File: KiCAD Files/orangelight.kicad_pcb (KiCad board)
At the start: 2 copper layers, 17.5 x 26 mm, 6 parts, among them J1 REV_JST_SMD, J2 REV_JST_SMD, U1 K230_Rewired, U2 ZDSD04GLGEAG, U3 HC-FPC-0_5-22P-CXH20, U4 K4E8E324ED-EGCG

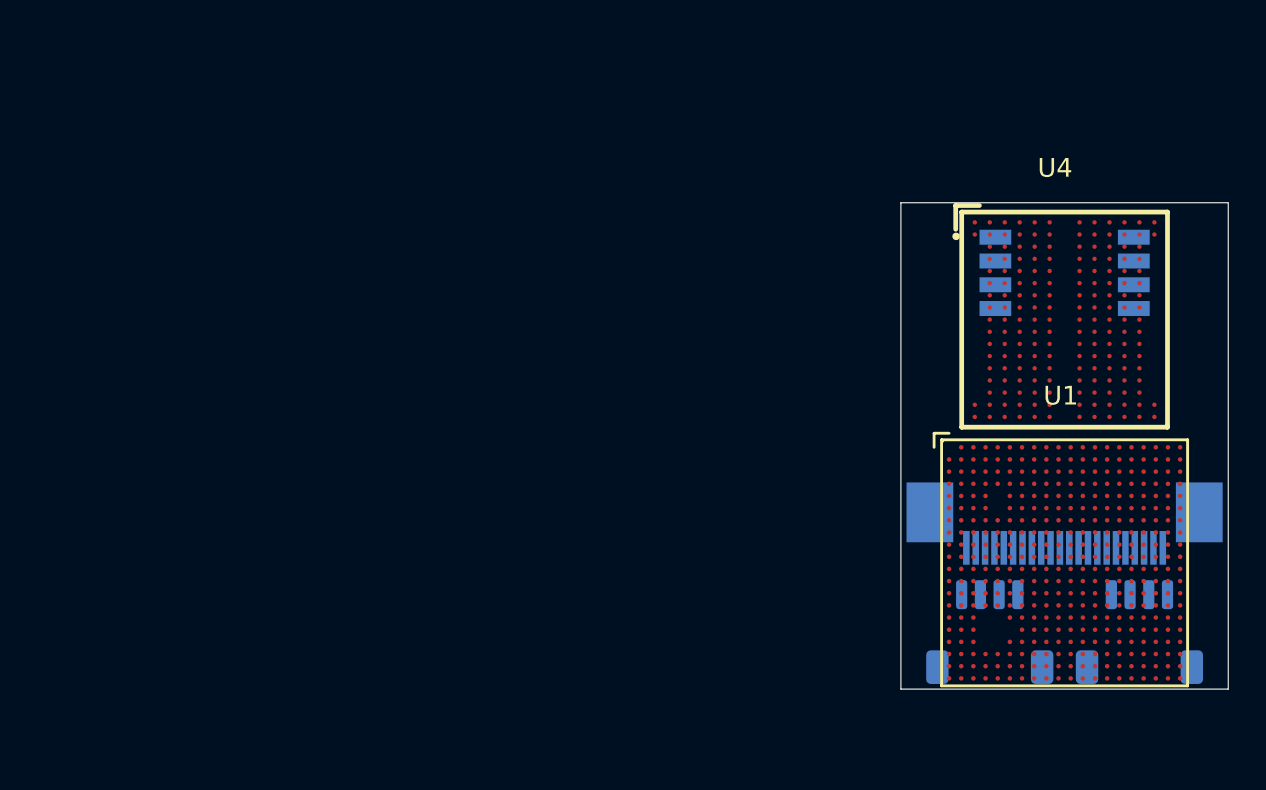
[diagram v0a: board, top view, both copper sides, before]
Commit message: more peripherals
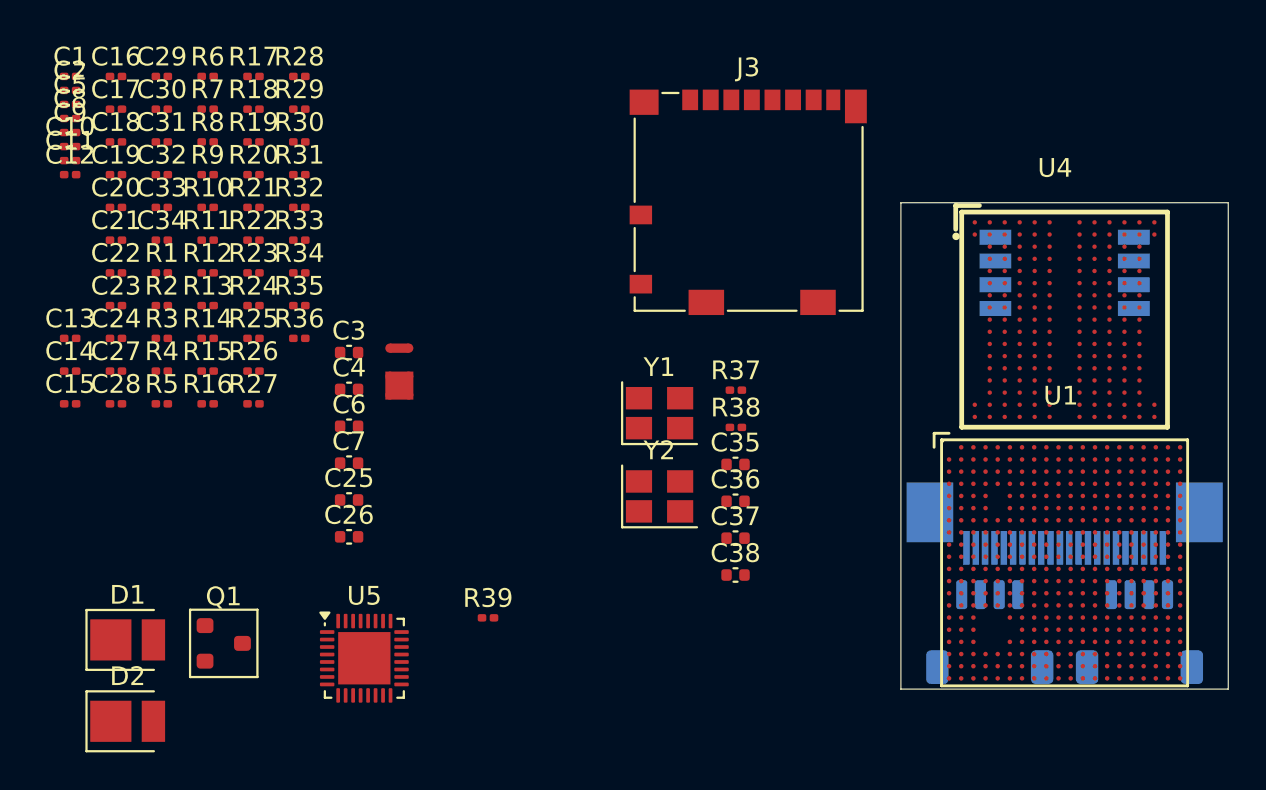
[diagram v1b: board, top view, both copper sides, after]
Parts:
- added C1: 100nF, Capacitor_SMD:C_0201_0603Metric, F.Cu at (-53.2, -26.0)
- added C10: 100nF, Capacitor_SMD:C_0201_0603Metric, F.Cu at (-53.2, -22.2)
- added C11: 100nF, Capacitor_SMD:C_0201_0603Metric, F.Cu at (-53.2, -21.5)
- added C12: 100nF, Capacitor_SMD:C_0201_0603Metric, F.Cu at (-53.2, -20.8)
- added C13: 100nF, Capacitor_SMD:C_0201_0603Metric, F.Cu at (-53.2, -12.0)
- added C14: 100nF, Capacitor_SMD:C_0201_0603Metric, F.Cu at (-53.2, -10.2)
- added C15: 100nF, Capacitor_SMD:C_0201_0603Metric, F.Cu at (-53.2, -8.50)
- added C16: 100nF, Capacitor_SMD:C_0201_0603Metric, F.Cu at (-50.7, -26.0)
- added C17: 100nF, Capacitor_SMD:C_0201_0603Metric, F.Cu at (-50.7, -24.2)
- added C18: 100nF, Capacitor_SMD:C_0201_0603Metric, F.Cu at (-50.7, -22.5)
- added C19: 100nF, Capacitor_SMD:C_0201_0603Metric, F.Cu at (-50.7, -20.8)
- added C2: 100nF, Capacitor_SMD:C_0201_0603Metric, F.Cu at (-53.2, -25.2)
- added C20: 100nF, Capacitor_SMD:C_0201_0603Metric, F.Cu at (-50.7, -19.0)
- added C21: 100nF, Capacitor_SMD:C_0201_0603Metric, F.Cu at (-50.7, -17.2)
- added C22: 100nF, Capacitor_SMD:C_0201_0603Metric, F.Cu at (-50.7, -15.5)
- added C23: 100nF, Capacitor_SMD:C_0201_0603Metric, F.Cu at (-50.7, -13.8)
- added C24: 100nF, Capacitor_SMD:C_0201_0603Metric, F.Cu at (-50.7, -12.0)
- added C25: 22uF, Capacitor_SMD:C_0402_1005Metric, F.Cu at (-38.2, -3.36)
- added C26: 4.7uF, Capacitor_SMD:C_0402_1005Metric, F.Cu at (-38.2, -1.39)
- added C27: 100nF, Capacitor_SMD:C_0201_0603Metric, F.Cu at (-50.7, -10.2)
- added C28: 100nF, Capacitor_SMD:C_0201_0603Metric, F.Cu at (-50.7, -8.50)
- added C29: 100nF, Capacitor_SMD:C_0201_0603Metric, F.Cu at (-48.3, -26.0)
- added C3: 22uF, Capacitor_SMD:C_0402_1005Metric, F.Cu at (-38.2, -11.2)
- added C30: 100nF, Capacitor_SMD:C_0201_0603Metric, F.Cu at (-48.3, -24.2)
- added C31: 100nF, Capacitor_SMD:C_0201_0603Metric, F.Cu at (-48.3, -22.5)
- added C32: 100nF, Capacitor_SMD:C_0201_0603Metric, F.Cu at (-48.3, -20.8)
- added C33: 100nF, Capacitor_SMD:C_0201_0603Metric, F.Cu at (-48.3, -19.0)
- added C34: 100nF, Capacitor_SMD:C_0201_0603Metric, F.Cu at (-48.3, -17.2)
- added C35: 15pF, Capacitor_SMD:C_0402_1005Metric, F.Cu at (-17.6, -5.26)
- added C36: 15pF, Capacitor_SMD:C_0402_1005Metric, F.Cu at (-17.6, -3.29)
- added C37: 15pF, Capacitor_SMD:C_0402_1005Metric, F.Cu at (-17.6, -1.32)
- added C38: 15pF, Capacitor_SMD:C_0402_1005Metric, F.Cu at (-17.6, 0.65)
- added C4: 4.7uF, Capacitor_SMD:C_0402_1005Metric, F.Cu at (-38.2, -9.27)
- added C5: 100nF, Capacitor_SMD:C_0201_0603Metric, F.Cu at (-53.2, -24.5)
- added C6: 22uF, Capacitor_SMD:C_0402_1005Metric, F.Cu at (-38.2, -7.30)
- added C7: 4.7uF, Capacitor_SMD:C_0402_1005Metric, F.Cu at (-38.2, -5.33)
- added C8: 100nF, Capacitor_SMD:C_0201_0603Metric, F.Cu at (-53.2, -23.8)
- added C9: 100nF, Capacitor_SMD:C_0201_0603Metric, F.Cu at (-53.2, -23.0)
- added D1: LED, LED_SMD:LED_PLCC_2835, F.Cu at (-50.1, 4.12)
- added D2: LED, LED_SMD:LED_PLCC_2835, F.Cu at (-50.1, 8.47)
- added J3: Micro_SD_Card_Det2, Connector_Card:microSD_HC_Molex_104031-0811, F.Cu at (-16.9, -19.3)
- added NT1: NetTie_2, NetTie:NetTie-2_SMD_Pad0.5mm, F.Cu at (-35.6, -11.5)
- added NT2: NetTie_4, NetTie:NetTie-4_SMD_Pad0.5mm, F.Cu at (-35.6, -9.47)
- added Q1: 2N7002, PCM_Package_TO_SOT_SMD_AKL:SOT-23, F.Cu at (-44.9, 4.30)
- added R1: 240R, Resistor_SMD:R_0201_0603Metric, F.Cu at (-48.3, -15.5)
- added R10: 120R, Resistor_SMD:R_0201_0603Metric, F.Cu at (-45.8, -19.0)
- added R11: 120R, Resistor_SMD:R_0201_0603Metric, F.Cu at (-45.8, -17.2)
- added R12: 120R, Resistor_SMD:R_0201_0603Metric, F.Cu at (-45.8, -15.5)
- added R13: 120R, Resistor_SMD:R_0201_0603Metric, F.Cu at (-45.8, -13.8)
- added R14: 120R, Resistor_SMD:R_0201_0603Metric, F.Cu at (-45.8, -12.0)
- added R15: 120R, Resistor_SMD:R_0201_0603Metric, F.Cu at (-45.8, -10.2)
- added R16: 120R, Resistor_SMD:R_0201_0603Metric, F.Cu at (-45.8, -8.50)
- added R17: 120R, Resistor_SMD:R_0201_0603Metric, F.Cu at (-43.4, -26.0)
- added R18: 120R, Resistor_SMD:R_0201_0603Metric, F.Cu at (-43.4, -24.2)
- added R19: 120R, Resistor_SMD:R_0201_0603Metric, F.Cu at (-43.4, -22.5)
- added R2: 240R, Resistor_SMD:R_0201_0603Metric, F.Cu at (-48.3, -13.8)
- added R20: 120R, Resistor_SMD:R_0201_0603Metric, F.Cu at (-43.4, -20.8)
- added R21: 120R, Resistor_SMD:R_0201_0603Metric, F.Cu at (-43.4, -19.0)
- added R22: 120R, Resistor_SMD:R_0201_0603Metric, F.Cu at (-43.4, -17.2)
- added R23: 120R, Resistor_SMD:R_0201_0603Metric, F.Cu at (-43.4, -15.5)
- added R24: 120R, Resistor_SMD:R_0201_0603Metric, F.Cu at (-43.4, -13.8)
- added R25: 120R, Resistor_SMD:R_0201_0603Metric, F.Cu at (-43.4, -12.0)
- added R26: 120R, Resistor_SMD:R_0201_0603Metric, F.Cu at (-43.4, -10.2)
- added R27: 120R, Resistor_SMD:R_0201_0603Metric, F.Cu at (-43.4, -8.50)
- added R28: 120R, Resistor_SMD:R_0201_0603Metric, F.Cu at (-40.9, -26.0)
- added R29: 120R, Resistor_SMD:R_0201_0603Metric, F.Cu at (-40.9, -24.2)
- added R3: 120R, Resistor_SMD:R_0201_0603Metric, F.Cu at (-48.3, -12.0)
- added R30: 120R, Resistor_SMD:R_0201_0603Metric, F.Cu at (-40.9, -22.5)
- added R31: 120R, Resistor_SMD:R_0201_0603Metric, F.Cu at (-40.9, -20.8)
- added R32: 120R, Resistor_SMD:R_0201_0603Metric, F.Cu at (-40.9, -19.0)
- added R33: 120R, Resistor_SMD:R_0201_0603Metric, F.Cu at (-40.9, -17.2)
- added R34: 120R, Resistor_SMD:R_0201_0603Metric, F.Cu at (-40.9, -15.5)
- added R35: 120R, Resistor_SMD:R_0201_0603Metric, F.Cu at (-40.9, -13.8)
- added R36: 240R, Resistor_SMD:R_0201_0603Metric, F.Cu at (-40.9, -12.0)
- added R37: 1M, Resistor_SMD:R_0201_0603Metric, F.Cu at (-17.6, -9.23)
- added R38: 1M, Resistor_SMD:R_0201_0603Metric, F.Cu at (-17.6, -7.24)
- added R39: 200R, Resistor_SMD:R_0201_0603Metric, F.Cu at (-30.8, 2.94)
- added R4: 120R, Resistor_SMD:R_0201_0603Metric, F.Cu at (-48.3, -10.2)
- added R5: 120R, Resistor_SMD:R_0201_0603Metric, F.Cu at (-48.3, -8.50)
- added R6: 120R, Resistor_SMD:R_0201_0603Metric, F.Cu at (-45.8, -26.0)
- added R7: 120R, Resistor_SMD:R_0201_0603Metric, F.Cu at (-45.8, -24.2)
- added R8: 120R, Resistor_SMD:R_0201_0603Metric, F.Cu at (-45.8, -22.5)
- added R9: 120R, Resistor_SMD:R_0201_0603Metric, F.Cu at (-45.8, -20.8)
- added U5: RT9992ZQW, Package_DFN_QFN:Texas_RSN_WQFN-32-1EP_4x4mm_P0.4mm_EP2.8x2.8mm, F.Cu at (-37.4, 5.10)
- added Y1: 32.768KHz, Crystal:Crystal_SMD_Abracon_ABM8AIG-4Pin_3.2x2.5mm, F.Cu at (-21.6, -8.00)
- added Y2: 32.768KHz, Crystal:Crystal_SMD_Abracon_ABM8AIG-4Pin_3.2x2.5mm, F.Cu at (-21.6, -3.55)
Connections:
- J1 pad 3: unconnected-(J1-3.3V-Pad3) -> +3V3
- J1 pad 4: unconnected-(J1-GND-Pad4) -> GND
- J2 pad 3: unconnected-(J2-3.3V-Pad3) -> +3V3
- J2 pad 4: unconnected-(J2-GND-Pad4) -> GND
- U2 pad 1: Net-(U1C-QSPI_D2) -> Net-(U1C-MMC0_D2)
- U2 pad 2: Net-(U1C-QSPI_D3) -> Net-(U1C-MMC0_D3)
- U2 pad 3: Net-(U1C-QSPI_CLK) -> Net-(U1C-MMC0_CLK)
- U2 pad 4: unconnected-(U2-GND-Pad4) -> GND
- U2 pad 5: Net-(U1C-QSPI_CS) -> Net-(U1C-MMC0_CMD)
- U2 pad 6: Net-(U1C-QSPI_D0) -> Net-(U1C-MMC0_D0)
- U2 pad 7: Net-(U1C-QSPI_D1) -> Net-(U1C-MMC0_D1)
- U2 pad 8: unconnected-(U2-VDD-Pad8) -> +3V3
- U4 pad A10: unconnected-(U4-VDD1-PadA10) -> DDR_VDD1
- U4 pad A11: unconnected-(U4-VDDQ-PadA11) -> DDR_VDDQ
- U4 pad A3: unconnected-(U4-VDD1-PadA3) -> DDR_VDD1
- U4 pad A4: unconnected-(U4-VDD1-PadA4) -> DDR_VDD1
- U4 pad A5: unconnected-(U4-VDD1-PadA5) -> DDR_VDD1
- U4 pad A6: unconnected-(U4-VDD1-PadA6) -> DDR_VDD1
- U4 pad A8: unconnected-(U4-VDD2-PadA8) -> DDR_VDD2
- U4 pad A9: unconnected-(U4-VDD2-PadA9) -> DDR_VDD2
- U4 pad B12: unconnected-(U4-VSSQ-PadB12) -> GND
- U4 pad B2: unconnected-(U4-VSS-PadB2) -> GND
- U4 pad B3: unconnected-(U4-ZQ-PadB3) -> Net-(U4-ZQ)
- U4 pad B5: unconnected-(U4-VSS-PadB5) -> GND
- U4 pad B6: unconnected-(U4-VSSQ-PadB6) -> GND
- U4 pad C12: unconnected-(U4-VDDQ-PadC12) -> DDR_VDDQ
- U4 pad C3: unconnected-(U4-VSSCA-PadC3) -> GND
- U4 pad C5: unconnected-(U4-VSS-PadC5) -> GND
- U4 pad C6: unconnected-(U4-VSSQ-PadC6) -> GND
- U4 pad D12: unconnected-(U4-VSSQ-PadD12) -> GND
- U4 pad D3: unconnected-(U4-VSSCA-PadD3) -> GND
- U4 pad D4: unconnected-(U4-VDD2-PadD4) -> DDR_VDD2
- U4 pad D5: unconnected-(U4-VDD2-PadD5) -> DDR_VDD2
- U4 pad D6: unconnected-(U4-VDD2-PadD6) -> DDR_VDD2
- U4 pad E12: unconnected-(U4-VDDQ-PadE12) -> DDR_VDDQ
- U4 pad E4: unconnected-(U4-VSS-PadE4) -> GND
- U4 pad E5: unconnected-(U4-VSS-PadE5) -> GND
- U4 pad E6: unconnected-(U4-VSSQ-PadE6) -> GND
- U4 pad E8: unconnected-(U4-VDDQ-PadE8) -> DDR_VDDQ
- U4 pad F12: unconnected-(U4-VSSQ-PadF12) -> GND
- U4 pad F2: unconnected-(U4-VDDCA-PadF2) -> DDR_VDDCA
- U4 pad F4: unconnected-(U4-VSSCA-PadF4) -> GND
- U4 pad F5: unconnected-(U4-VSS-PadF5) -> GND
- U4 pad F6: unconnected-(U4-VSSQ-PadF6) -> GND
- U4 pad G12: unconnected-(U4-VDDQ-PadG12) -> DDR_VDDQ
- U4 pad G2: unconnected-(U4-VDDCA-PadG2) -> DDR_VDDCA
- U4 pad G3: unconnected-(U4-VSSCA-PadG3) -> GND
- U4 pad G4: unconnected-(U4-VSSCA-PadG4) -> GND
- U4 pad G5: unconnected-(U4-VDD2-PadG5) -> DDR_VDD2
- U4 pad G6: unconnected-(U4-VSSQ-PadG6) -> GND
- U4 pad G9: unconnected-(U4-VSSQ-PadG9) -> GND
- U4 pad H10: unconnected-(U4-VSSQ-PadH10) -> GND
- U4 pad H11: unconnected-(U4-VDDQ-PadH11) -> DDR_VDDQ
- U4 pad H12: unconnected-(U4-VDD2-PadH12) -> DDR_VDD2
- U4 pad H2: unconnected-(U4-VSS-PadH2) -> GND
- U4 pad H3: unconnected-(U4-VDDCA-PadH3) -> DDR_VDDCA
- U4 pad H4: unconnected-(U4-VRef(CA)-PadH4) -> /RAM/DDR.VREF_CA
- U4 pad H5: unconnected-(U4-VDD2-PadH5) -> DDR_VDD2
- U4 pad H6: unconnected-(U4-VDD2-PadH6) -> DDR_VDD2
- U4 pad H8: unconnected-(U4-VDDQ-PadH8) -> DDR_VDDQ
- U4 pad H9: unconnected-(U4-VDDQ-PadH9) -> DDR_VDDQ
- U4 pad J10: unconnected-(U4-VDDQ-PadJ10) -> DDR_VDDQ
- U4 pad J11: unconnected-(U4-VRef(DQ)-PadJ11) -> /RAM/DDR.VREF_DQ
- U4 pad J12: unconnected-(U4-VSS-PadJ12) -> GND
- U4 pad J2: unconnected-(U4-CK_N-PadJ2) -> /RAM/DDR_CK-
- U4 pad J3: unconnected-(U4-CK_P-PadJ3) -> /RAM/DDR_CK+
- U4 pad J4: unconnected-(U4-VSSCA-PadJ4) -> GND
- U4 pad J5: unconnected-(U4-VDD2-PadJ5) -> DDR_VDD2
- U4 pad J6: unconnected-(U4-VDD2-PadJ6) -> DDR_VDD2
- U4 pad J8: unconnected-(U4-ODT(1)-PadJ8) -> /RAM/DDR.ODT
- U4 pad J9: unconnected-(U4-VDDQ-PadJ9) -> DDR_VDDQ
- U4 pad K10: unconnected-(U4-VSSQ-PadK10) -> GND
- U4 pad K11: unconnected-(U4-VDDQ-PadK11) -> DDR_VDDQ
- U4 pad K12: unconnected-(U4-VDD2-PadK12) -> DDR_VDD2
- U4 pad K2: unconnected-(U4-VSS-PadK2) -> GND
- U4 pad K3: unconnected-(U4-CKE-PadK3) -> /RAM/DDR_CKE
- U4 pad K5: unconnected-(U4-VDD2-PadK5) -> DDR_VDD2
- U4 pad K6: unconnected-(U4-VDD2-PadK6) -> DDR_VDD2
- U4 pad K8: unconnected-(U4-VDDQ-PadK8) -> DDR_VDDQ
- U4 pad L12: unconnected-(U4-VDDQ-PadL12) -> DDR_VDDQ
- U4 pad L2: unconnected-(U4-VDDCA-PadL2) -> DDR_VDDCA
- U4 pad L3: unconnected-(U4-CS_N-PadL3) -> /RAM/DDR.CS
- U4 pad L5: unconnected-(U4-VDD2-PadL5) -> DDR_VDD2
- U4 pad L6: unconnected-(U4-VSS-PadL6) -> GND
- U4 pad L9: unconnected-(U4-VSSQ-PadL9) -> GND
- U4 pad M12: unconnected-(U4-VSSQ-PadM12) -> GND
- U4 pad M2: unconnected-(U4-VDDCA-PadM2) -> DDR_VDDCA
- U4 pad M4: unconnected-(U4-VSSCA-PadM4) -> GND
- U4 pad M5: unconnected-(U4-VSSCA-PadM5) -> GND
- U4 pad M6: unconnected-(U4-VSSQ-PadM6) -> GND
- U4 pad N12: unconnected-(U4-VDDQ-PadN12) -> DDR_VDDQ
- U4 pad N4: unconnected-(U4-VSS-PadN4) -> GND
- U4 pad N5: unconnected-(U4-VSS-PadN5) -> GND
- U4 pad N6: unconnected-(U4-VSSQ-PadN6) -> GND
- U4 pad N8: unconnected-(U4-VDDQ-PadN8) -> DDR_VDDQ
- U4 pad P12: unconnected-(U4-VSSQ-PadP12) -> GND
- U4 pad P3: unconnected-(U4-VSSCA-PadP3) -> GND
- U4 pad P4: unconnected-(U4-VDD2-PadP4) -> DDR_VDD2
- U4 pad P5: unconnected-(U4-VDD2-PadP5) -> DDR_VDD2
- U4 pad P6: unconnected-(U4-VDD2-PadP6) -> DDR_VDD2
- U4 pad R12: unconnected-(U4-VDDQ-PadR12) -> DDR_VDDQ
- U4 pad R4: unconnected-(U4-VSS-PadR4) -> GND
- U4 pad R5: unconnected-(U4-VSS-PadR5) -> GND
- U4 pad R6: unconnected-(U4-VSSQ-PadR6) -> GND
- U4 pad T12: unconnected-(U4-VSSQ-PadT12) -> GND
- U4 pad T2: unconnected-(U4-VSS-PadT2) -> GND
- U4 pad T3: unconnected-(U4-VSS-PadT3) -> GND
- U4 pad T4: unconnected-(U4-VSS-PadT4) -> GND
- U4 pad T5: unconnected-(U4-VSS-PadT5) -> GND
- U4 pad T6: unconnected-(U4-VSSQ-PadT6) -> GND
- U4 pad U10: unconnected-(U4-VDD1-PadU10) -> DDR_VDD1
- U4 pad U11: unconnected-(U4-VDDQ-PadU11) -> DDR_VDDQ
- U4 pad U3: unconnected-(U4-VDD1-PadU3) -> DDR_VDD1
- U4 pad U4: unconnected-(U4-VDD1-PadU4) -> DDR_VDD1
- U4 pad U5: unconnected-(U4-VDD1-PadU5) -> DDR_VDD1
- U4 pad U6: unconnected-(U4-VDD1-PadU6) -> DDR_VDD1
- U4 pad U8: unconnected-(U4-VDD2-PadU8) -> DDR_VDD2
- U4 pad U9: unconnected-(U4-VDD2-PadU9) -> DDR_VDD2
